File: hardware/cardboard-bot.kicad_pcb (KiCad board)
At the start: 2 copper layers, 80 x 46 mm, 110 parts, among them J1 USB-C CHARGE, J10 ESC PWR 2, J2 I2C, J3 MOTOR L, J4 MOTOR R, J5 OUT1, J6 OUT2, J7 IO3, J8 IO21, J9 ESC PWR 1, Q1 HYG015N03LS1C2 DSG, Q2 HYG015N03LS1C2 CHG, Q3 CJAB35P03, Q4 AO3401A, Q5 AO3401A, SW1 POWER, U1 IP2320, U2 HY2120-CB, U3 TPS54202DDCR, U4 XIAO ESP32-C3, U5 DRV8833PWPR, U7 HY2213-BB3A, U8 HY2213-BB3A

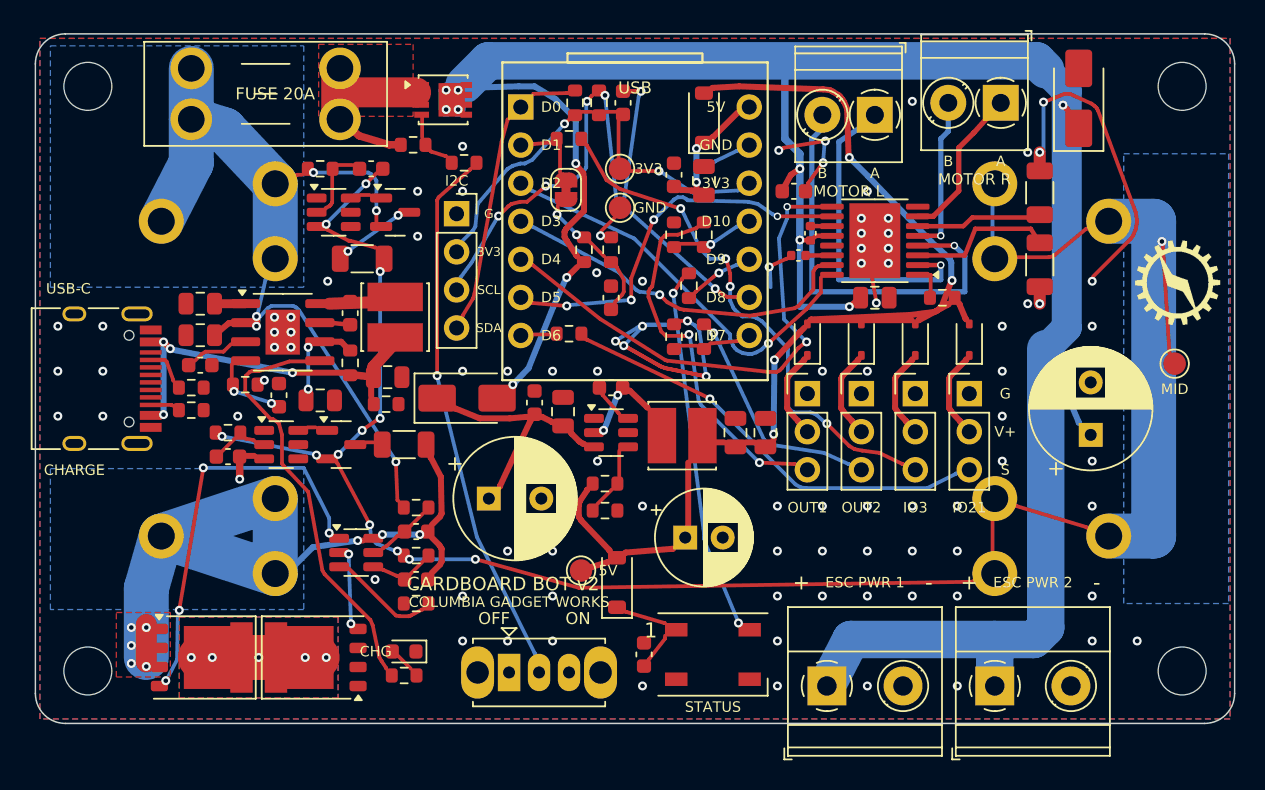
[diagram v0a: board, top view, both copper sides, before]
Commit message: Simplify rev A: off-board power switch, no balancing, LED strip pads
- SW1: 18 AWG wire pads for a 10 A+ panel switch; Q3, R11, R12 and the slide switch removed
- Cell balancers (U7, U8, Q4, Q5, R29-R32, C32, C33) removed; BMS still cuts at 4.28 V
- NTC replaced by a fixed 10k (R33); NTC fits the same pads
- D2: SMF10CA (Preferred) instead of SMAJ10A
- C1, C20: 10 uF instead of 22 uF
- J11: pads for one LED cut from a WS2812B strip; TP4 removed
- Re-routed, DRC clean; new gerbers, BOM, CPL, previews
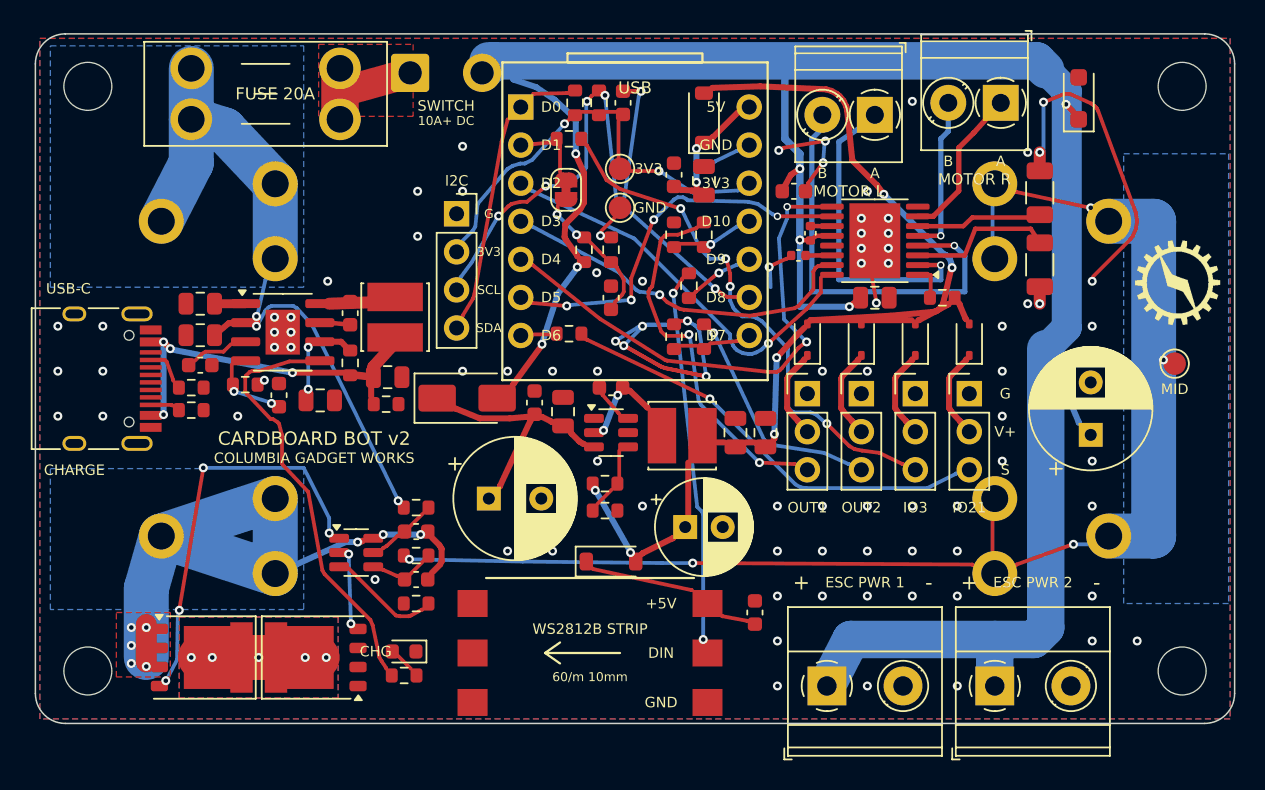
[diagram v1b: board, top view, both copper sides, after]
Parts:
- removed C32, C33: 100nF, Capacitor_SMD:C_0603_1608Metric
- removed D9: XL-5050RGBC-2812B-S, LED_SMD:LED_WS2812B_PLCC4_5.0x5.0mm_P3.2mm
- removed Q3: CJAB35P03, Package_SO:Vishay_PowerPAK_1212-8_Single
- removed Q4, Q5: AO3401A, Package_TO_SOT_SMD:SOT-23
- removed R11: 100k, Resistor_SMD:R_0603_1608Metric
- removed R12: 10k, Resistor_SMD:R_0603_1608Metric
- removed R29, R31: 100R, Resistor_SMD:R_0603_1608Metric
- removed R30, R32: 100R, Resistor_SMD:R_1206_3216Metric
- removed TP4: +5V, TestPoint:TestPoint_Pad_D1.5mm
- removed U7, U8: HY2213-BB3A, Package_TO_SOT_SMD:SOT-23-6
- added J11: LED STRIP, cgw:WS2812B_Strip_1LED, F.Cu at (137.0, 141.3)
- C1, C20: value 22uF -> 10uF
- D2: value SMAJ10A -> SMF10CA; footprint Diode_SMD:D_SMA -> Diode_SMD:D_SOD-123F
- R33: renamed from TH1; value 10k B3380 -> 10k
- SW1: value POWER -> POWER SW; footprint Button_Switch_THT:SW_Slide_SPDT_Straight_CK_OS102011MS2Q -> Connector_Wire:SolderWire-0.75sqmm_1x02_P4.8mm_D1.25mm_OD2.3mm
- moved SW1 40.5 mm to (125.0, 102.6)
- moved C30 7.91 mm to (148.0, 138.6)
- moved D10 1.46 mm to (138.4, 135.2), turned to 0 degrees
- moved C19 0.70 mm to (143.3, 132.9)
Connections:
- SW1 pad 1: (no net) -> VFUSE
- SW1 pad 2: PSW_SW -> VSYS
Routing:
- net MID: track 122.8 -> 81.9 mm, vias 13 -> 5
- net PSW_SW: track 34.6 -> 0.00 mm, vias 1 -> 0
- net VSYS: track 160.1 -> 152.1 mm, vias 11 -> 7
- net BAT+: track 53.9 -> 46.0 mm, vias 5 -> 3
- net B_NEG: track 49.3 -> 42.0 mm, vias 9 -> 8
- net VFUSE: track 13.0 -> 8.26 mm
- net BAL1_D: track 4.12 -> 0.00 mm, vias 2 -> 0
- net LED_VDD: track 4.74 -> 8.55 mm
- net BAL1_VDD: track 3.37 -> 0.00 mm
- net +5V: track 67.4 -> 64.3 mm, vias 4 -> 6
- net PSW_G: track 2.47 -> 0.00 mm
- net BAL2_VDD: track 1.83 -> 0.00 mm
- net LED_DIN: track 23.8 -> 24.5 mm
- net BAL1_G: track 0.65 -> 0.00 mm
- net BAL2_G: track 0.55 -> 0.00 mm
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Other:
- board text added: "10A+ DC"
- board text added: "SWITCH"
- board text removed: "5V"
- board text removed: "OFF"
- board text removed: "ON"
- board text removed: "STATUS"

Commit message: Rev B board: 2S/3S LiPo on a screw terminal, two DRV8870s, smaller
- Removed the 18650 clips, USB-C charger and BMS; battery comes in on a 5.08 mm
  screw terminal, then the 20 A fuse and the switch pads
- Everything on the battery rail rated above 3S: two DRV8870 drivers (45 V, 2.5 A limit),
  SMAJ13A clamp, 25 V bulk capacitors; battery sense is now pack / 6
- 10k pull-downs on all four motor inputs and all three outputs
- Motor terminals on opposite edges (LEFT MOTOR / RIGHT MOTOR), ESC power on the right
- 60 x 46 mm (was 80 x 46), nothing on the back; 20 BOM lines, 3 Extended
- Routed, DRC clean; new gerbers, BOM, CPL, schematic, previews and docs
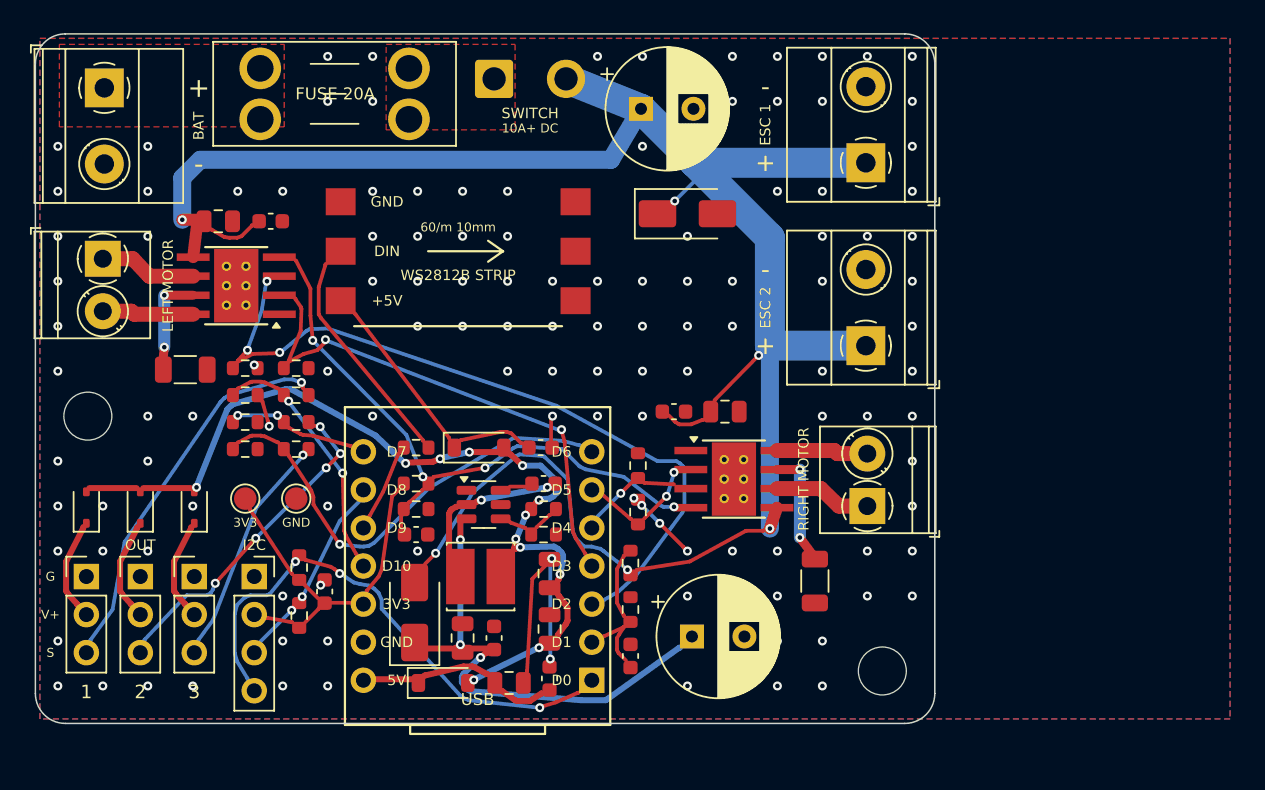
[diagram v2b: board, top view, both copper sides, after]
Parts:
- removed BT1, BT2, BT3, BT4: 18650 clip, cgw:Clip_MY-18650-01
- removed C19: 220uF 16V, Capacitor_THT:CP_Radial_D6.3mm_P2.50mm
- removed C20, C23: 10uF, Capacitor_SMD:C_0805_2012Metric
- removed C21, C22, C24, C30, C31: 100nF, Capacitor_SMD:C_0603_1608Metric
- removed C25: 2.2uF, Capacitor_SMD:C_0402_1005Metric
- removed C26: 10nF, Capacitor_SMD:C_0402_1005Metric
- removed C27: 470uF 16V, Capacitor_THT:CP_Radial_D8.0mm_P3.50mm
- removed D10: 1N4148W, Diode_SMD:D_SOD-123
- removed D8: 1N5819WS, Diode_SMD:D_SOD-323
- removed H3, H4: MountingHole_3.2mm_M3, MountingHole:MountingHole_3.2mm_M3
- removed J11: LED STRIP, cgw:WS2812B_Strip_1LED
- removed JP1: VBAT>IO3, Jumper:SolderJumper-2_P1.3mm_Bridged_RoundedPad1.0x1.5mm
- removed L2: 10uH 2.35A, Inductor_SMD:L_Cenker_CKCS4030
- removed LOGO1: CGW_Logo_6mm, cgw:CGW_Logo_6mm
- removed Q1: HYG015N03LS1C2 DSG, Package_DFN_QFN:PQFN-8-EP_6x5mm_P1.27mm_Generic
- removed Q2: HYG015N03LS1C2 CHG, Package_DFN_QFN:PQFN-8-EP_6x5mm_P1.27mm_Generic
- removed R22: 1k, Resistor_SMD:R_0603_1608Metric
- removed R23, R33: 10k, Resistor_SMD:R_0603_1608Metric
- removed R24, R25, R26: 330R, Resistor_SMD:R_0603_1608Metric
- removed R27: 300k, Resistor_SMD:R_0603_1608Metric
- removed R28: 100k, Resistor_SMD:R_0603_1608Metric
- removed TP5: +3V3, TestPoint:TestPoint_Pad_D1.5mm
- removed TP6: GND, TestPoint:TestPoint_Pad_D1.5mm
- removed TP7: MID, TestPoint:TestPoint_Pad_D1.5mm
- removed U5: DRV8833PWPR, Package_SO:HTSSOP-16-1EP_4.4x5mm_P0.65mm_EP3.4x5mm_Mask2.46x2.31mm
- added C12: 100nF, Capacitor_SMD:C_0603_1608Metric, F.Cu at (139.7, 141.5)
- added C9: 10uF, Capacitor_SMD:C_0805_2012Metric, F.Cu at (131.6, 143.3)
- added R11: 10k, Resistor_SMD:R_0603_1608Metric, F.Cu at (114.0, 122.3)
- added R12: 10k, Resistor_SMD:R_0603_1608Metric, F.Cu at (117.4, 122.3)
- added R5: 100k, Resistor_SMD:R_0603_1608Metric, F.Cu at (139.7, 135.3)
- added R6: 20k, Resistor_SMD:R_0603_1608Metric, F.Cu at (139.7, 138.4)
- added TP1: +3V3, TestPoint:TestPoint_Pad_D1.5mm, F.Cu at (114.0, 131.0)
- added TP2: GND, TestPoint:TestPoint_Pad_D1.5mm, F.Cu at (117.4, 131.0)
- C1: value 10uF -> 470uF 25V; footprint Capacitor_SMD:C_0805_2012Metric -> Capacitor_THT:CP_Radial_D8.0mm_P3.50mm
- C13: value 470uF 16V -> 100nF; footprint Capacitor_THT:CP_Radial_D8.0mm_P3.50mm -> Capacitor_SMD:C_0603_1608Metric
- C16: value 100nF -> 10uF; footprint Capacitor_SMD:C_0603_1608Metric -> Capacitor_SMD:C_0805_2012Metric
- C17, C18: value 22uF -> 100nF; footprint Capacitor_SMD:C_0805_2012Metric -> Capacitor_SMD:C_0603_1608Metric
- C2: value 22uF -> 470uF 25V; footprint Capacitor_SMD:C_0805_2012Metric -> Capacitor_THT:CP_Radial_D8.0mm_P3.50mm
- C5: value 10uF -> 100nF; footprint Capacitor_SMD:C_0805_2012Metric -> Capacitor_SMD:C_0603_1608Metric
- C6, C7: value 100nF -> 22uF; footprint Capacitor_SMD:C_0603_1608Metric -> Capacitor_SMD:C_0805_2012Metric
- D1: value RED -> SMAJ13A; footprint LED_SMD:LED_0603_1608Metric -> Diode_SMD:D_SMA
- D2: value SMF10CA -> SS34; footprint Diode_SMD:D_SOD-123F -> Diode_SMD:D_SMA
- D3: value SS34 -> B5819W; footprint Diode_SMD:D_SMA -> Diode_SMD:D_SOD-123
- D4: value B5819W -> 1N5819WS; footprint Diode_SMD:D_SOD-123 -> Diode_SMD:D_SOD-323
- D7: value 1N5819WS -> 1N4148W; footprint Diode_SMD:D_SOD-323 -> Diode_SMD:D_SOD-123
- J1: value USB-C CHARGE -> BATTERY; footprint Connector_USB:USB_C_Receptacle_HRO_TYPE-C-31-M-12 -> TerminalBlock_Phoenix:TerminalBlock_Phoenix_MKDS-1,5-2-5.08_1x02_P5.08mm_Horizontal
- J10: value ESC PWR 2 -> LED STRIP; footprint TerminalBlock_Phoenix:TerminalBlock_Phoenix_MKDS-1,5-2-5.08_1x02_P5.08mm_Horizontal -> cgw:WS2812B_Strip_1LED
- J3: value MOTOR L -> LEFT MOTOR
- J4: value MOTOR R -> RIGHT MOTOR
- J7: value IO3 -> OUT3
- J8: value IO21 -> ESC PWR 1; footprint Connector_PinHeader_2.54mm:PinHeader_1x03_P2.54mm_Vertical -> TerminalBlock_Phoenix:TerminalBlock_Phoenix_MKDS-1,5-2-5.08_1x02_P5.08mm_Horizontal
- J9: value ESC PWR 1 -> ESC PWR 2
- L1: value 2.2uH 4.8A -> 10uH 2.35A
- LOGO2: value CGW_Logo_Small_Back -> CGW_Logo; footprint cgw:CGW_Logo_Small_Back -> cgw:CGW_Logo
- R1: value 5.1k -> 75k
- R10: value 2k -> 33k
- R13: value 75k -> 10k
- R15, R16: value 4.7k -> 1k
- R17: value 10k -> 1k
- R18, R19: value 0.1R -> 10k; footprint Resistor_SMD:R_1206_3216Metric -> Resistor_SMD:R_0603_1608Metric
- R2: value 5.1k -> 10k
- R20, R9: value 1k -> 10k
- R21: value 10k -> 330R
- R3: value 5.1k -> 4.7k
- R4: value 1R -> 4.7k
- R7: value 1k -> 0.1R; footprint Resistor_SMD:R_0603_1608Metric -> Resistor_SMD:R_1206_3216Metric
- R8: value 330R -> 0.1R; footprint Resistor_SMD:R_0603_1608Metric -> Resistor_SMD:R_1206_3216Metric
- U1: value IP2320 -> TPS54202DDCR; footprint Package_SO:SOIC-8-1EP_3.9x4.9mm_P1.27mm_EP2.29x3mm -> Package_TO_SOT_SMD:TSOT-23-6
- U2: value HY2120-CB -> XIAO ESP32-C3; footprint Package_TO_SOT_SMD:SOT-23-6 -> cgw:XIAO_Socket
- U3: value TPS54202DDCR -> DRV8870DDAR; footprint Package_TO_SOT_SMD:TSOT-23-6 -> Package_SO:Texas_HTSOP-8-1EP_3.9x4.9mm_P1.27mm_EP2.95x4.9mm_Mask2.4x3.1mm_ThermalVias
- U4: value XIAO ESP32-C3 -> DRV8870DDAR; footprint cgw:XIAO_Socket -> Package_SO:Texas_HTSOP-8-1EP_3.9x4.9mm_P1.27mm_EP2.95x4.9mm_Mask2.4x3.1mm_ThermalVias
- moved D2 56.0 mm to (125.3, 138.6)
- moved R19 55.2 mm to (114.0, 125.9), turned to 0 degrees
- moved R18 53.7 mm to (114.0, 124.1), turned to 0 degrees
- moved J3 52.4 mm to (104.5, 115.0), turned to -90 degrees
- moved J5 49.6 mm to (103.4, 136.2)
- moved J6 49.6 mm to (107.0, 136.2)
- moved J7 49.6 mm to (110.6, 136.2)
- moved D4 48.7 mm to (103.4, 131.6)
- moved J10 46.1 mm to (128.2, 114.5), turned to 180 degrees
- moved D5 45.9 mm to (107.0, 131.6)
- moved D6 45.9 mm to (110.6, 131.6)
- moved R17 44.3 mm to (117.4, 127.7), turned to 0 degrees
- moved H2 43.8 mm to (156.5, 142.5)
- moved C2 39.6 mm to (143.8, 140.2), turned to 0 degrees
- moved D1 34.8 mm to (143.5, 112.0), turned to 0 degrees
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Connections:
- C1 pad 1: VBUS -> VSYS
- C10 pad 1: BMS_VDD -> +5V_XIAO
- C10 pad 2: B_NEG -> GND
- C11 pad 1: BMS_VC -> +3V3
- C11 pad 2: B_NEG -> GND
- C13 pad 1: VHOLD -> DRV_VREF
- C14 pad 1: VHOLD -> VSYS
- C15 pad 1: VHOLD -> VSYS
- C16 pad 1: BUCK_BST -> VSYS
- C16 pad 2: BUCK_SW -> GND
- C17 pad 1: +5V -> VSYS
- C18 pad 1: +5V -> LED_VDD
- C2 pad 1: CHG_VSYS -> VHOLD
- C3 pad 1: BAT+ -> VHOLD
- C4 pad 1: CHG_BST -> VHOLD
- C4 pad 2: CHG_LX -> GND
- C5 pad 1: CHG_VIN -> BUCK_BST
- C5 pad 2: GND -> BUCK_SW
- C6 pad 1: CHG_VSET -> +5V
- C7 pad 1: CHG_NTC -> +5V
- D1 pad 1: GND -> VSYS
- D1 pad 2: CHG_LED_A -> GND
- D2 pad 1: VSYS -> VHOLD
- D2 pad 2: GND -> VSYS
- D3 pad 1: VHOLD -> +5V_XIAO
- D3 pad 2: VSYS -> +5V
- D4 pad 1: +5V_XIAO -> OUT1_VP
- D5 pad 1: OUT1_VP -> OUT2_VP
- D6 pad 1: OUT2_VP -> OUT3_VP
- D7 pad 1: IO3_VP -> LED_VDD
- J10 pad 1: VSYS -> LED_VDD
- J10 pad 2: GND -> LED_DIN
- J7 pad 2: IO3_VP -> OUT3_VP
- J7 pad 3: IO3_SIG -> OUT3_SIG
- J8 pad 1: GND -> VSYS
- J8 pad 2: IO21_VP -> GND
- L1 pad 1: VBUS -> BUCK_SW
- L1 pad 2: CHG_LX -> +5V
- R1 pad 1: CC1 -> +5V
- R1 pad 2: GND -> BUCK_FB
- R10 pad 1: GND -> DRV_VREF
- R10 pad 2: BMS_CS -> GND
- R13 pad 1: +5V -> BIN1
- R13 pad 2: BUCK_FB -> GND
- R14 pad 1: BUCK_FB -> BIN2
- R15 pad 1: +3V3 -> IO10
- R15 pad 2: SDA -> OUT1_SIG
- R16 pad 1: +3V3 -> IO20
- R16 pad 2: SCL -> OUT2_SIG
- R17 pad 1: +5V -> IO21
- R17 pad 2: DRV_SLEEP -> OUT3_SIG
- R18 pad 1: DRV_AISEN -> IO10
- R19 pad 1: DRV_BISEN -> IO20
- R2 pad 1: CC2 -> BUCK_FB
- R20 pad 1: IO10 -> IO21
- R20 pad 2: OUT1_SIG -> GND
- R21 pad 1: IO10 -> LED_DIN3
- R21 pad 2: GND -> LED_DIN
- R3 pad 1: VBUS -> +3V3
- R3 pad 2: GND -> SDA
- R4 pad 1: VBUS -> +3V3
- R4 pad 2: CHG_VIN -> SCL
- R7 pad 1: CHG_LED -> ISEN_L
- R7 pad 2: CHG_LED_A -> GND
- R8 pad 1: BAT+ -> ISEN_R
- R8 pad 2: BMS_VDD -> GND
- R9 pad 1: MID -> +3V3
- R9 pad 2: BMS_VC -> DRV_VREF
- U1 pad 1: CHG_VSYS -> GND
- U1 pad 2: BAT+ -> BUCK_SW
- U1 pad 3: CHG_VSET -> VHOLD
- U1 pad 4: CHG_NTC -> BUCK_FB
- U1 pad 5: CHG_LED -> (no net)
- U1 pad 6: CHG_VIN -> BUCK_BST
- U2 pad 1: BMS_DO -> SDA
- U2 pad 2: BMS_CO -> VBAT_SNS
- U2 pad 3: BMS_CS -> AIN1
- U2 pad 4: BMS_VC -> AIN2
- U2 pad 5: BMS_VDD -> BIN1
- U2 pad 6: B_NEG -> BIN2
- U3 pad 2: BUCK_SW -> AIN2
- U3 pad 3: VHOLD -> AIN1
- U3 pad 4: BUCK_FB -> DRV_VREF
- U3 pad 5: (no net) -> VSYS
- U3 pad 6: BUCK_BST -> MOTL_A
- U4 pad 1: SDA -> GND
- U4 pad 2: IO3 -> BIN2
- U4 pad 3: AIN1 -> BIN1
- U4 pad 4: AIN2 -> DRV_VREF
- U4 pad 5: BIN1 -> VSYS
- U4 pad 6: BIN2 -> MOTR_A
- U4 pad 7: IO21 -> ISEN_R
- U4 pad 8: IO20 -> MOTR_B
- U4 pad 9: SCL -> GND
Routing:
- net MID: track 81.9 -> 0.00 mm, vias 5 -> 0
- net GND: track 70.2 -> 21.1 mm, vias 91 -> 127
- net BAT+: track 46.0 -> 0.00 mm, vias 3 -> 0
- net B_NEG: track 42.0 -> 0.00 mm, vias 8 -> 0
- net DRV_VREF: track 0.00 -> 37.3 mm, vias 0 -> 4
- net IO3_SIG: track 34.0 -> 0.00 mm, vias 4 -> 0
- net BIN1: track 33.9 -> 5.18 mm, vias 2 -> 1
- net IO21_SIG: track 28.3 -> 0.00 mm, vias 1 -> 0
- net IO21: track 1.15 -> 28.4 mm, vias 0 -> 1
- net CHG_LED: track 27.0 -> 0.00 mm
- net BMS_DO: track 26.1 -> 0.00 mm, vias 4 -> 0
- net SCL: track 34.3 -> 10.6 mm, vias 5 -> 2
- net AIN1: track 26.1 -> 49.3 mm, vias 1 -> 3
- net VBUS: track 23.2 -> 0.00 mm, vias 4 -> 0
- net MOTL_B: track 28.1 -> 6.11 mm, vias 1 -> 0
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- added copper zone on F.Cu, net BAT+
- removed copper zone on B.Cu, net BAT+
- removed copper zone on B.Cu, net BMS_DRAIN
- removed copper zone on F.Cu, net BMS_DRAIN
- removed copper zone on B.Cu, net B_NEG
- removed copper zone on F.Cu, net B_NEG
- removed copper zone on B.Cu, net MID
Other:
- board size 80 x 46 mm -> 60 x 46 mm
- board text added: "1"
- board text added: "2"
- board text added: "2S or 3S LiPo only"
- board text added: "3"
- board text added: "BAT"
- board text added: "COLUMBIA GADGET WORKS rev B"
- board text added: "ESC 1"
- board text added: "ESC 2"
- board text added: "LEFT MOTOR"
- board text added: "OUT"
- board text added: "RIGHT MOTOR"
- board text added: "github.com/ColumbiaGadgetWorks/cardboard-bot-v2"
- board text removed: "2S 18650: flat top, unprotected, 20A+, matched pairs"
- board text removed: "A"
- board text removed: "B"
- board text removed: "CELL A"
- board text removed: "CELL B"
- board text removed: "CHARGE"
- board text removed: "CHG"
- board text removed: "COLUMBIA GADGET WORKS"
- board text removed: "ESC PWR 1"
- board text removed: "ESC PWR 2"
- board text removed: "IO21"
- board text removed: "IO3"
- board text removed: "MID"
- board text removed: "MOTOR L"
- board text removed: "MOTOR R"
- board text removed: "OUT1"
- board text removed: "OUT2"
- board text removed: "TRIM ALL LEADS FLUSH + KAPTON TAPE BEFORE FITTING CELLS"
- board text removed: "USB-C"
- board text removed: "github.com/ColumbiaGadgetWorks/cardboard-bot-v2 rev A"
